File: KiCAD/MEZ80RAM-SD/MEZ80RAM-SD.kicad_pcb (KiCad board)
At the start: 2 copper layers, 50.8 x 58.4 mm, 21 parts, among them J1 EMUZ80_0, J2 EMUZ80, J3 SD Card slot, J4 ext SPI, U1 Z80CPU, U2 TC551001, U3 MCP23S08-xP

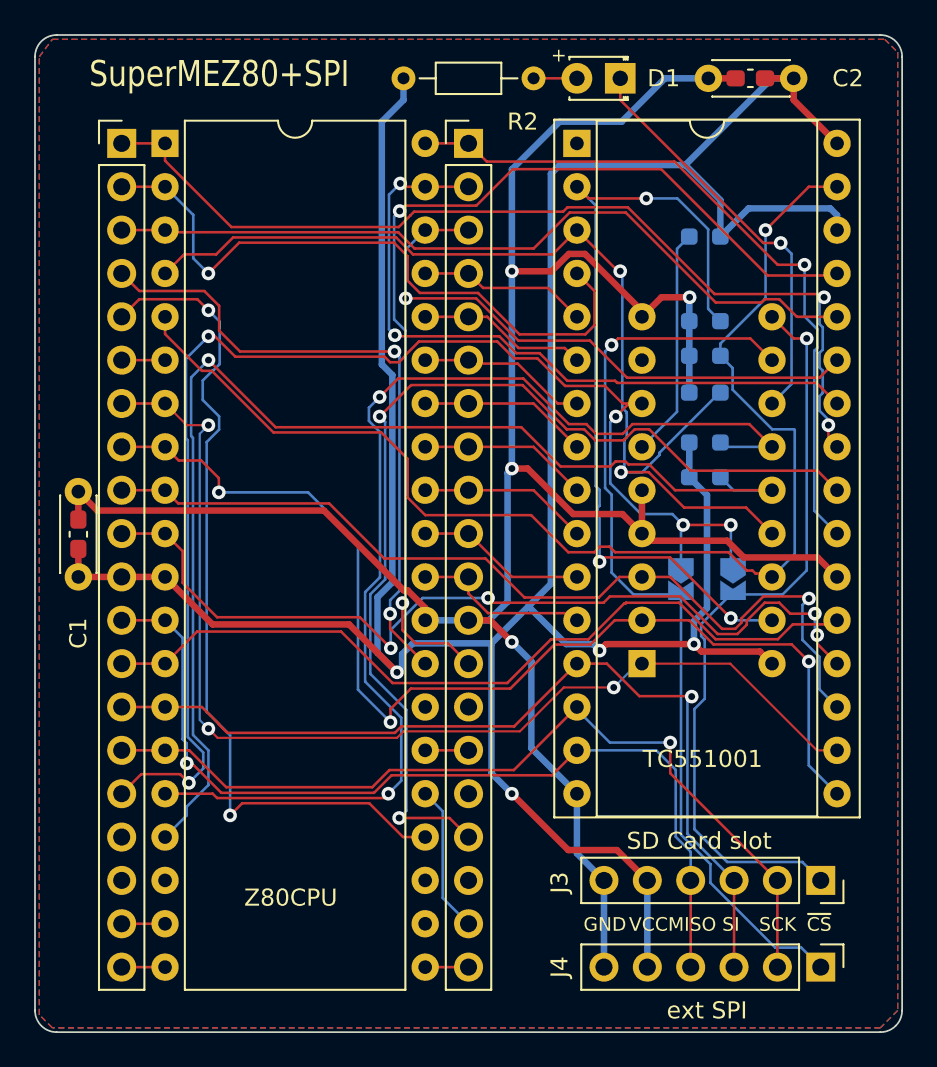
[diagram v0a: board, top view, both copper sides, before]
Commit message: Update MEZ80RAM-SD to verion 0.9
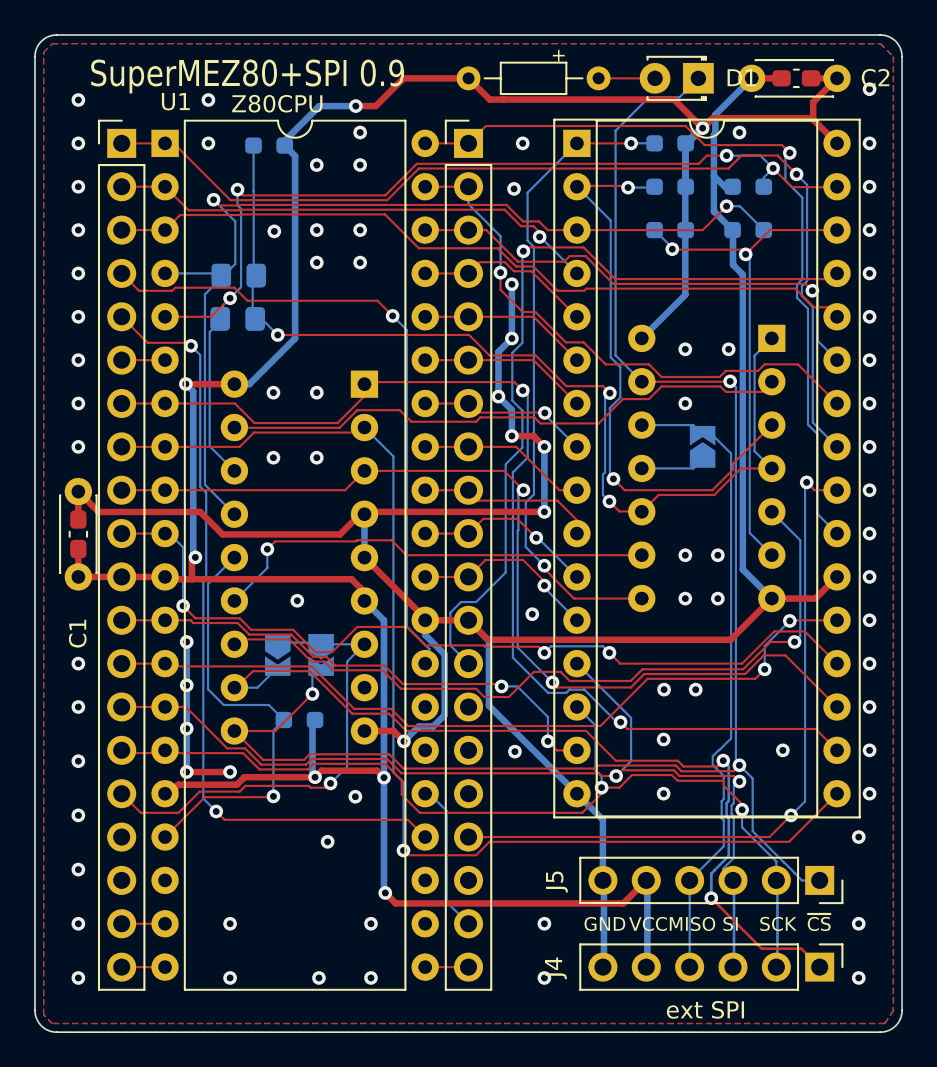
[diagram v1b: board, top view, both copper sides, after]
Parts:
- removed J3: SD Card slot, Connector_PinSocket_2.54mm:PinSocket_1x06_P2.54mm_Vertical
- removed JP1, JP2: Jumper_2_Open, Jumper:SolderJumper-2_P1.3mm_Open_TrianglePad1.0x1.5mm
- removed R1, R5, R6: 10K, Resistor_SMD:R_0603_1608Metric_Pad0.98x0.95mm_HandSolder
- added D2: 1N4001, Diode_SMD:D_0805_2012Metric_Pad1.15x1.40mm_HandSolder, B.Cu at (131.3, 85.2)
- added D3: 1N4001, Diode_SMD:D_0805_2012Metric_Pad1.15x1.40mm_HandSolder, B.Cu at (131.3, 87.8)
- added J5: SD Card slot, Connector_PinSocket_2.54mm:PinSocket_1x06_P2.54mm_Vertical, F.Cu at (165.4, 120.7)
- added JP1 CS0: Jumper_2_Open, Jumper:SolderJumper-2_P1.3mm_Open_TrianglePad1.0x1.5mm, B.Cu at (136.1, 107.4)
- added JP2 CS1: Jumper_2_Open, Jumper:SolderJumper-2_P1.3mm_Open_TrianglePad1.0x1.5mm, B.Cu at (133.6, 107.4)
- added JP3      D2 - MISO: Jumper_2_Open, Jumper:SolderJumper-2_P1.3mm_Open_TrianglePad1.0x1.5mm, B.Cu at (158.5, 95.2)
- added R10: 10K, Resistor_SMD:R_0603_1608Metric_Pad0.98x0.95mm_HandSolder, B.Cu at (156.6, 82.5)
- added R11: 10K, Resistor_SMD:R_0603_1608Metric_Pad0.98x0.95mm_HandSolder, B.Cu at (156.6, 77.5)
- added R8: 1K, Resistor_SMD:R_0603_1608Metric_Pad0.98x0.95mm_HandSolder, B.Cu at (133.1, 77.6)
- added R9: 10K, Resistor_SMD:R_0603_1608Metric_Pad0.98x0.95mm_HandSolder, B.Cu at (156.6, 80.0)
- added REF**: OSHW-Logo2_7.3x6mm_SilkScreen, Symbol:OSHW-Logo2_7.3x6mm_SilkScreen, B.Cu at (138.5, 123.2)
- added U4: 74LS125, Package_DIP:DIP-14_W7.62mm, B.Cu at (162.6, 88.9)
- U2: value TC551001 -> AS6C4008
- U3: value MCP23S08-xP -> MCP23S08
- moved R7 27.7 mm to (134.9, 111.3), turned to 180 degrees
- moved U3 23.1 mm to (138.7, 91.6), turned to 180 degrees
- moved R4 10.2 mm to (161.2, 80.0)
- moved R3 9.86 mm to (161.2, 82.5)
- moved D1 4.58 mm to (158.2, 73.7)
- moved R2 3.81 mm to (144.8, 73.7)
- moved C4 2.69 mm to (164.0, 73.7)
- moved C2 2.54 mm to (166.4, 73.7)
- moved J4 0.06 mm to (165.4, 125.7)
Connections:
- D1 pad 1: ~{LED} -> ~{CS0}
- J1 pad 12: D2 -> /D2
- J4 pad 4: D2 -> MISO
- U1 pad 12: D2 -> /D2
- U1 pad 16: ~{INT} -> VCC
- U2 pad 1: unconnected-(U2-NC-Pad1) -> A18
- U2 pad 15: D2 -> /D2
- U2 pad 30: VCC -> A17
- U3 pad 12: ~{LED} -> BANK1
- U3 pad 13: ~{INT} -> BANK2
- U3 pad 17: A16 -> BANK0
- U3 pad 6: Net-(U3-~{RESET}) -> VCC
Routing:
- net ~{INT}: track 67.3 -> 0.00 mm, vias 2 -> 0
- net Net-(D2-A): track 0.00 -> 58.9 mm, vias 0 -> 3
- net ~{CS0}: track 44.8 -> 97.2 mm, vias 1 -> 3
- net ~{CS}: track 79.1 -> 27.6 mm, vias 5 -> 1
- net D2: track 54.2 -> 3.79 mm, vias 1 -> 0
- net BANK1: track 0.00 -> 44.6 mm, vias 0 -> 1
- net ~{NMI}: track 69.6 -> 25.6 mm
- net A18: track 0.00 -> 37.9 mm, vias 0 -> 2
- net MISO: track 0.00 -> 37.7 mm
- net BANK0: track 0.00 -> 33.7 mm
- net /D2: track 0.00 -> 30.7 mm, vias 0 -> 2
- net A17: track 0.00 -> 30.2 mm, vias 0 -> 2
- net BANK2: track 0.00 -> 26.3 mm, vias 0 -> 1
- net ~{LED}: track 24.3 -> 0.00 mm, vias 1 -> 0
- net GND: track 138.7 -> 161.0 mm, vias 4 -> 89
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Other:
- board text added: "@hanyazou April 9, 2023"
- board text added: "SuperMEZ80+SPI 0.9"
- board text removed: "MCP23S08"
- board text removed: "SuperMEZ80 + SPI Rev 0.8 Mezzanine board for EMUZ80 Sat Feb 25, 2023"
- board text removed: "SuperMEZ80+SPI"
